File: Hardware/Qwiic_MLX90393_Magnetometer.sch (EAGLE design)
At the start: 24 parts, among them U1 MLX90393_MAGNETOMETER

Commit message: post qc checklist changes
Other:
- note added: "v10"
- note removed: "v01"
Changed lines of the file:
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@@
 <sheet>
 <plain>
-<text x="203.2" y="113.538" size="1.778" layer="97">Address selection jumpers</text>
-<text x="236.22" y="7.62" size="2.54" layer="94">v01</text>
+<text x="203.2" y="113.538" size="1.778" layer="97" font="vector">Address selection jumpers</text>
+<text x="236.22" y="7.62" size="2.54" layer="94">v10</text>
 <text x="165.608" y="11.176" size="2.54" layer="94">R. Reynolds</text>
-<text x="5.08" y="177.8" size="3.81" layer="97">MLX90393 Breakout</text>
-<text x="178.308" y="146.558" size="1.778" layer="97" align="top-left">SJ2 pulls up the SCK and SDA lines
+<text x="5.08" y="177.8" size="3.81" layer="97" font="vector">MLX90393 Breakout</text>
+<text x="178.308" y="146.558" size="1.778" layer="97" font="vector" align="top-left">SJ2 pulls up the SCK and SDA lines
 for I2C operation</text>
-<text x="5.08" y="175.26" size="2.032" layer="97" align="top-left">MODES:
+<text x="5.08" y="175.26" size="2.032" layer="97" font="vector" align="top-left">MODES:
   I2C:
     Leave the copper-connected jumpers
@@
 <wire x1="0" y1="66.04" x2="147.32" y2="66.04" width="0.1524" layer="97" style="longdash"/>
 <wire x1="147.32" y1="66.04" x2="147.32" y2="35.56" width="0.1524" layer="97" style="longdash"/>
-<text x="5.08" y="132.08" size="3.175" layer="97">Magnetometer Circuitry</text>
-<text x="5.08" y="58.42" size="3.175" layer="97">User Ports</text>
-<text x="5.08" y="55.88" size="2.032" layer="97" align="top-left">VCC must be 2.2-3.6V</text>
+<text x="5.08" y="132.08" size="3.175" layer="97" font="vector">Magnetometer Circuitry</text>
+<text x="5.08" y="58.42" size="3.175" layer="97" font="vector">User Ports</text>
+<text x="111.76" y="137.16" size="2.032" layer="97" font="vector" align="top-left">VCC must be 2.2-3.6V</text>
 <wire x1="147.32" y1="66.04" x2="248.92" y2="66.04" width="0.1524" layer="97" style="longdash"/>
 <wire x1="0" y1="139.7" x2="91.44" y2="139.7" width="0.1524" layer="97" style="longdash"/>
 <wire x1="91.44" y1="185.42" x2="91.44" y2="139.7" width="0.1524" layer="97" style="longdash"/>
-<text x="128.016" y="140.716" size="1.778" layer="97">SJ1 Controls I2C/SPI
+<text x="128.016" y="140.716" size="1.778" layer="97" font="vector">SJ1 Controls I2C/SPI
 Closed (Default): I2C
 Open: SPI</text>
@@
 <wire x1="213.36" y1="129.54" x2="208.28" y2="129.54" width="0.2032" layer="97"/>
 <wire x1="208.28" y1="129.54" x2="208.28" y2="132.08" width="0.2032" layer="97"/>
-<text x="209.804" y="130.048" size="1.27" layer="97">A1</text>
-<text x="214.884" y="130.048" size="1.27" layer="97">A0</text>
-<text x="219.964" y="130.048" size="1.27" layer="97">I2C Address</text>
-<text x="222.25" y="127.508" size="1.27" layer="97">0001100</text>
-<text x="222.25" y="124.968" size="1.27" layer="97">0001101</text>
-<text x="222.25" y="122.428" size="1.27" layer="97">0001110</text>
-<text x="222.25" y="120.142" size="1.27" layer="97">0001111</text>
+<text x="209.804" y="130.048" size="1.27" layer="97" font="vector">A1</text>
+<text x="214.884" y="130.048" size="1.27" layer="97" font="vector">A0</text>
+<text x="219.964" y="130.048" size="1.27" layer="97" font="vector">I2C Address</text>
+<text x="222.25" y="127.508" size="1.27" layer="97" font="vector">0001100</text>
+<text x="222.25" y="124.968" size="1.27" layer="97" font="vector">0001101</text>
+<text x="222.25" y="122.428" size="1.27" layer="97" font="vector">0001110</text>
+<text x="222.25" y="120.142" size="1.27" layer="97" font="vector">0001111</text>
 <wire x1="233.68" y1="127" x2="208.28" y2="127" width="0.2032" layer="97"/>
 <wire x1="208.28" y1="127" x2="208.28" y2="124.46" width="0.2032" layer="97"/>
@@
 <wire x1="213.36" y1="129.54" x2="213.36" y2="119.38" width="0.2032" layer="97"/>
 <wire x1="218.44" y1="129.54" x2="218.44" y2="119.38" width="0.2032" layer="97"/>
-<text x="209.042" y="127.508" size="1.27" layer="97">GND</text>
-<text x="214.122" y="127.508" size="1.27" layer="97">GND</text>
-<text x="209.042" y="124.968" size="1.27" layer="97">GND</text>
-<text x="214.122" y="122.428" size="1.27" layer="97">GND</text>
-<text x="214.122" y="124.968" size="1.27" layer="97">VDD</text>
-<text x="209.042" y="122.428" size="1.27" layer="97">VDD</text>
-<text x="209.042" y="119.888" size="1.27" layer="97">VDD</text>
-<text x="214.122" y="119.888" size="1.27" layer="97">VDD</text>
-<text x="8.89" y="158.75" size="2.032" layer="97" align="top-left">SPI 4-WIRE:
+<text x="209.042" y="127.508" size="1.27" layer="97" font="vector">GND</text>
+<text x="214.122" y="127.508" size="1.27" layer="97" font="vector">GND</text>
+<text x="209.042" y="124.968" size="1.27" layer="97" font="vector">GND</text>
+<text x="214.122" y="122.428" size="1.27" layer="97" font="vector">GND</text>
+<text x="214.122" y="124.968" size="1.27" layer="97" font="vector">VDD</text>
+<text x="209.042" y="122.428" size="1.27" layer="97" font="vector">VDD</text>
+<text x="209.042" y="119.888" size="1.27" layer="97" font="vector">VDD</text>
+<text x="214.122" y="119.888" size="1.27" layer="97" font="vector">VDD</text>
+<text x="8.89" y="158.75" size="2.032" layer="97" font="vector" align="top-left">SPI 4-WIRE:
   Jumpers SJ2 can be opened to
   remove pull-ups on the SPI lines.
   SJ1 must be open for SPI operation.</text>
-<text x="205.994" y="133.35" size="1.778" layer="97">I2C Addressing Table</text>
-<text x="199.898" y="81.788" size="1.778" layer="97">Default 7-bit I2C Adr: 0x0C</text>
+<text x="205.994" y="133.35" size="1.778" layer="97" font="vector">I2C Addressing Table</text>
+<text x="199.898" y="81.788" size="1.778" layer="97" font="vector">Default 7-bit I2C Adr: 0x0C</text>
 <text x="168.2496" y="6.731" size="2.54" layer="94">A. England</text>
 </plain>

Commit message: fixed version number
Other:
- note added: "v01"
- note removed: "v10"
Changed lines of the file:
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@@
 <plain>
 <text x="203.2" y="113.538" size="1.778" layer="97" font="vector">Address selection jumpers</text>
-<text x="236.22" y="7.62" size="2.54" layer="94">v10</text>
+<text x="236.22" y="7.62" size="2.54" layer="94">v01</text>
 <text x="165.608" y="11.176" size="2.54" layer="94">R. Reynolds</text>
 <text x="5.08" y="177.8" size="3.81" layer="97" font="vector">MLX90393 Breakout</text>

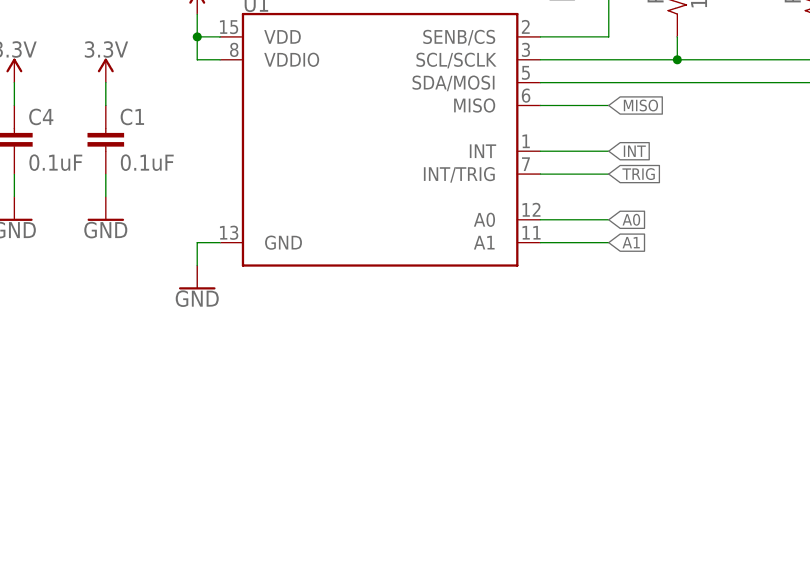
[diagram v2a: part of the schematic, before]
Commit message: updated footprint for magnetometer
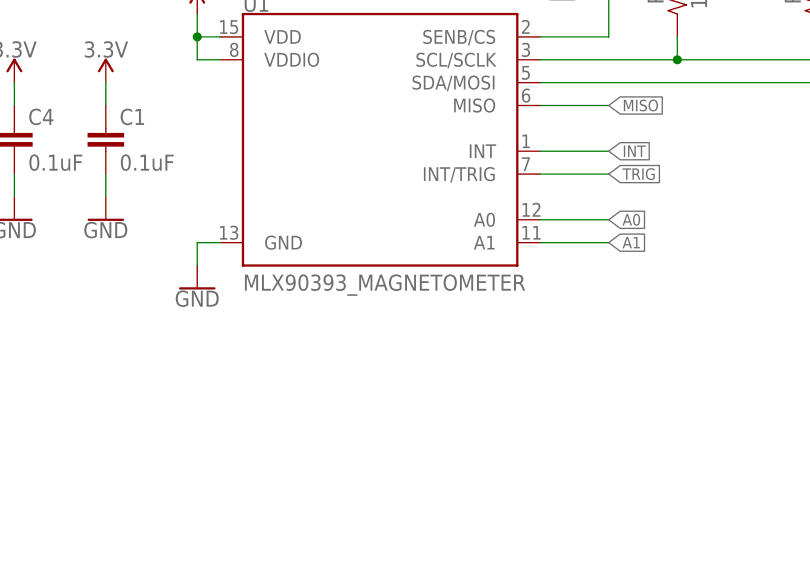
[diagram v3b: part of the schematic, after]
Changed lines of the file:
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@@
 </classes>
 <parts>
-<part name="U1" library="SparkFun-Sensors" deviceset="MLX90393_MAGNETOMETER" device="" value=""/>
+<part name="U1" library="SparkFun-Sensors" deviceset="MLX90393_MAGNETOMETER" device="" value="MLX90393_MAGNETOMETER"/>
 <part name="R1" library="SparkFun-Resistors" deviceset="10KOHM" device="-0603-1/10W-1%" value="10k"/>
 <part name="R2" library="SparkFun-Resistors" deviceset="10KOHM" device="-0603-1/10W-1%" value="10k"/>
